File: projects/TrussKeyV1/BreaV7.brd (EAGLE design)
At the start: 30.8 x 19 mm, 32 parts, among them J1 XF2L-0535-1, J2 XF2L-0535-1, Q1 ABM-16MHZ, SW1 LS12T2-T, SW2 EVQ11U09K, SW3 ESE31L11T, U2 TPS62200, X1 22-23-2021

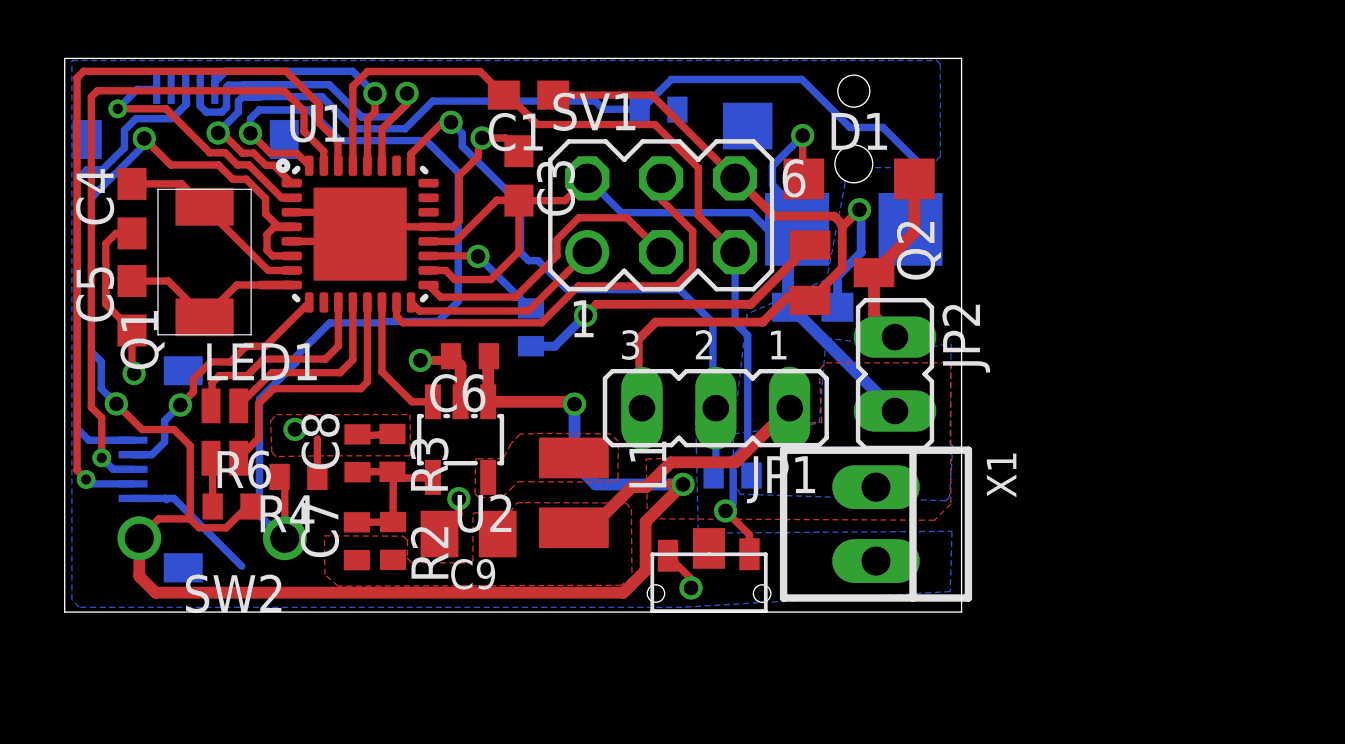
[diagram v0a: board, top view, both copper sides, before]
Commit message: Generate SP boards for Gen1
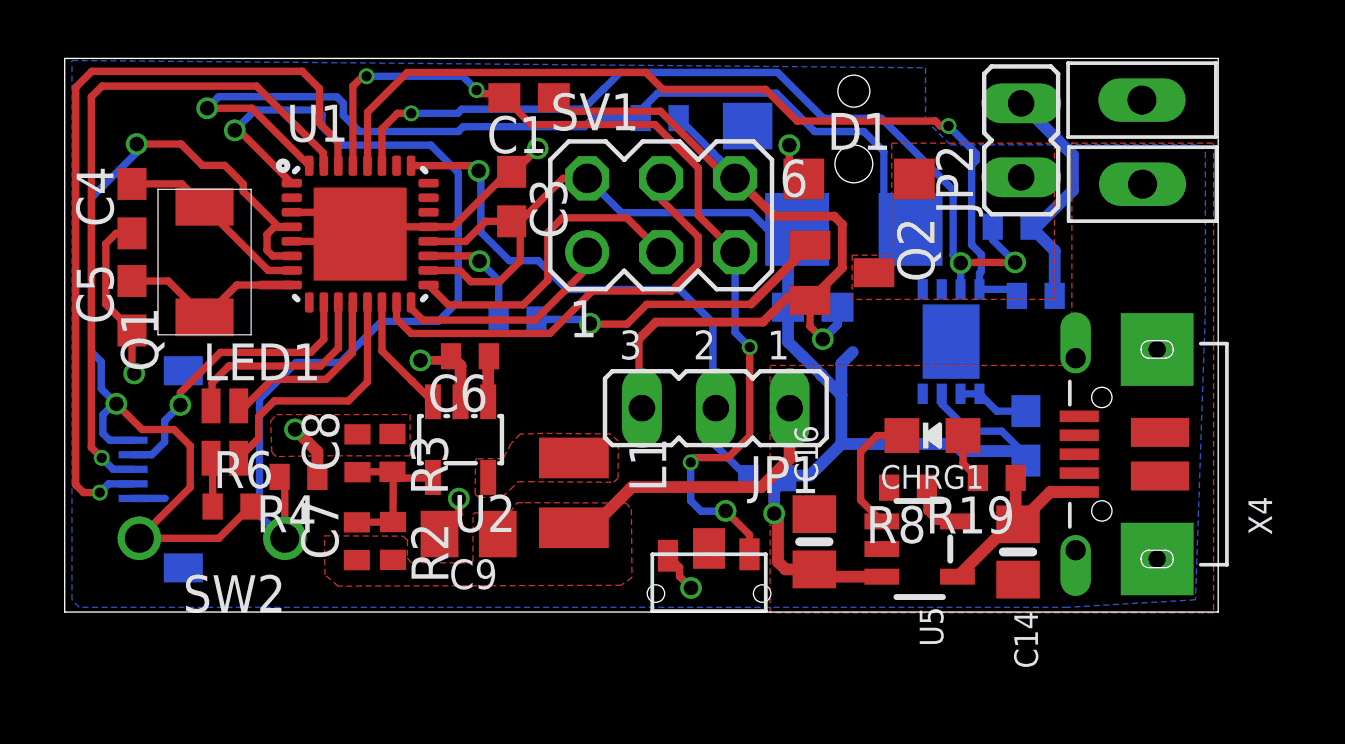
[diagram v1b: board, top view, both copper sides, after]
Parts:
- removed J1: XF2L-0535-1, adafruit:XF2L-0535-1
- added C14, C16: 10µF, microbuilder:0805-NO
- added C17: 1uF, rcl:C0603
- added CHRG1: ORANGE, microbuilder:CHIPLED_0805_NOOUTLINE
- added R15, R16: 10K, resistor:R0402
- added R19: 330, resistor:R0402
- added R8: 2K, resistor:R0402
- added U3: LC709203, NewPart:WDFN8
- added U5: MCP73831T-2ACI/OT, microbuilder:SOT23-5
- added X3: CON-1PIN, NewPart:CON-1PIN
- added X4: MicroB, microbuilder:4UCONN_20329
- R4: value 330 -> 1k
- R7: value 330 -> 1K
- X1: value 22-23-2021 -> CON-1PIN; device con-molex:22-23-2021 -> NewPart:CON-1PIN
- moved X1 17.2 mm to (37.0, 17.6), turned to 90 degrees
- moved JP2 9.13 mm to (32.9, 16.2), turned to 0 degrees
- moved R1 1.19 mm to (24.1, 4.57)
- moved C3 0.75 mm to (15.4, 14.2)
- moved R5 0.53 mm to (15.6, 10.0), turned to 0 degrees
- moved R7 0.29 mm to (20.5, 16.9)
- moved C1 0.09 mm to (16.0, 17.6)
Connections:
- removed net VBATSIM: J1.3, J2.1
- new net N$12: R8.1, U5.5
- new net N$16: CHRG1.A, R19.2
- new net N$17: CHRG1.C, U5.1
- new net N$7: C6.1, U2.1
- new net VBUS2: C14.1, R19.1, U5.4, X4.VBUS
- net DETSW: now also U1.32; no longer U1.1
- net GND: now also C14.2, C16.2, C17.1, R8.2, U3.1, U3.2, U3.9, U5.2, X3.P$1, X4.BASE@1, X4.BASE@2, X4.GND, X4.SPRT@1, X4.SPRT@2, X4.SPRT@3, X4.SPRT@4; no longer X1.2
- net LEDSOC: no longer J1.5
- net PWRSW: now also U1.1; no longer U1.32
- net REST: now also U1.10; no longer U1.9
- net SCL: now also R15.1, U3.8; no longer J1.1
- net SDA: now also R16.1, U3.7; no longer J1.2
- net VCC: now also C16.1, C17.2, J2.1, R15.2, R16.2, U3.3, U5.3, X1.P$1; no longer C6.1, U2.1, X1.1
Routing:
- net SCL: track 8.81 -> 30.7 mm
- net SDA: track 12.4 -> 30.3 mm, vias 1 -> 3
- net VBATSIM: track 16.3 -> 0.00 mm
- net LEDSOC: track 8.86 -> 0.00 mm, vias 1 -> 0
- net VBUS2: track 0.00 -> 7.01 mm
- net N$9: track 6.31 -> 0.00 mm
- net VCC: track 96.6 -> 91.7 mm, vias 5 -> 4
- net N$17: track 0.00 -> 4.34 mm
- net GND: track 61.7 -> 59.1 mm
- net RST: track 30.8 -> 32.9 mm, vias 1 -> 5
- net N$12: track 0.00 -> 2.00 mm
- net N$16: track 0.00 -> 1.67 mm
- net N$7: track 0.00 -> 1.58 mm
- net REST: track 8.90 -> 10.1 mm
- net N$3: track 20.6 -> 19.6 mm
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- added copper zone on layer 15, net GND
- added copper zone on layer 2, net GND
- added copper zone on layer 1, net N$9
- added copper zone on layer 15, net VCC
- removed copper zone on layer 1, net VCC
- removed copper zone on layer 16, net VCC
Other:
- board size 30.8 x 19 mm -> 39.6 x 19 mm
